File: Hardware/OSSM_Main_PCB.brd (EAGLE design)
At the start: 114.3 x 45.4 mm, 9 parts, among them J1 PJ-037AH, U1 LOLIN32_PRODUCTION

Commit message: Added Diode on 5V regulator
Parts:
- added D1: SS24FL, SS24FL:SODFL3617X108N
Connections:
- new net N$1: D1.A, PS1.3
- net 5V: now also D1.C; no longer PS1.3
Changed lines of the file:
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@@
 <attribute name="VALUE" x="55.245" y="52.07" size="1.27" layer="27" align="top-left"/>
+</element>
+<element name="D1" library="SS24FL" package="SODFL3617X108N" value="SS24FL" x="0" y="6.35" smashed="yes">
+<attribute name="DESCRIPTION" value=" Diode Schottky 40V 2A Surface Mount SOD-123F " x="0" y="6.35" size="1.778" layer="27" display="off"/>
+<attribute name="DIGI-KEY_PART_NUMBER" value="SS24FLCT-ND" x="0" y="6.35" size="1.778" layer="27" display="off"/>
+<attribute name="MF" value="ON Semiconductor" x="0" y="6.35" size="1.778" layer="27" display="off"/>
+<attribute name="MP" value="SS24FL" x="0" y="6.35" size="1.778" layer="27" display="off"/>
+<attribute name="NAME" x="-2.54" y="7.747" size="1.27" layer="25"/>
+<attribute name="PACKAGE" value="SOD-123 FL-2 ON Semiconductor" x="0" y="6.35" size="1.778" layer="27" display="off"/>
+<attribute name="PURCHASE-URL" value="https://pricing.snapeda.com/search/part/SS24FL/?ref=eda" x="0" y="6.35" size="1.778" layer="27" display="off"/>
+<attribute name="VALUE" x="-2.54" y="3.81" size="1.27" layer="27"/>
 </element>
 </elements>
@@
 </signal>
 <signal name="5V">
+<contactref element="D1" pad="C"/>
 <contactref element="U1" pad="15"/>
-<contactref element="PS1" pad="3"/>
-<wire x1="63.5" y1="54.9" x2="12.14" y2="74.93" width="0" layer="19" extent="1-1"/>
+<wire x1="-1.53" y1="6.35" x2="12.14" y2="74.93" width="0" layer="19" extent="1-1"/>
 </signal>
 <signal name="GND">
@@
 <wire x1="58.42" y1="54.9" x2="0" y2="41.91" width="0" layer="19" extent="1-1"/>
 </signal>
+<signal name="N$1">
+<contactref element="PS1" pad="3"/>
+<contactref element="D1" pad="A"/>
+<wire x1="1.53" y1="6.35" x2="63.5" y2="54.9" width="0" layer="19" extent="1-1"/>
+</signal>
 </signals>

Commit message: James' Attempt
Maybe made it better, maybe made it worse?
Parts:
- added C1: (no value), rcl:C050-024X044
- moved QWIIC_CONN 68.5 mm to (128.3, 53.3)
- moved STEPPER 66.8 mm to (91.4, 52.1)
- moved D1 64.5 mm to (54.6, 40.6), turned to 270 degrees
- moved 3.3V_CONN 64.4 mm to (134.6, 33.0), turned to 180 degrees
- moved MTR_CONN 61.8 mm to (100.3, 33.0), turned to 180 degrees
- moved IO_CONN 40.4 mm to (134.6, 72.4), turned to 180 degrees
- moved PS1 27.0 mm to (43.2, 36.8)
- moved GND_CONN 9.25 mm to (100.3, 72.4)
- moved J1 5.08 mm to (0.00, 36.8)
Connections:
- removed net VDD: STEPPER.10
- removed net VMOT: STEPPER.16
- new net N$10: MTR_CONN.4, STEPPER.13
- new net N$11: MTR_CONN.3, STEPPER.14
- new net N$12: IO_CONN.1, U1.13
- new net N$13: IO_CONN.2, U1.12
- new net N$14: IO_CONN.3, U1.11
- new net N$15: IO_CONN.4, U1.10
- new net N$16: IO_CONN.5, U1.9
- new net N$17: IO_CONN.6, U1.8
- new net N$2: STEPPER.1, U1.25
- new net N$3: STEPPER.2, U1.26
- new net N$4: STEPPER.3, U1.27
- new net N$5: STEPPER.4, U1.30
- new net N$6: STEPPER.7, U1.31
- new net N$7: STEPPER.8, U1.14
- new net N$8: MTR_CONN.6, STEPPER.11
- new net N$9: MTR_CONN.5, STEPPER.12
- net 24V: now also C1.2, STEPPER.16
- net 5V: now also STEPPER.10
- net GND: now also C1.1
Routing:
- net GND: track 0.00 -> 259.5 mm
- net 24V: track 0.00 -> 171.3 mm
- net 5V: track 0.00 -> 159.8 mm
- net N$12: track 0.00 -> 119.5 mm
- net N$13: track 0.00 -> 112.7 mm
- net N$14: track 0.00 -> 104.9 mm
- net N$15: track 0.00 -> 100.4 mm
- net 21_SDA: track 0.00 -> 96.0 mm
- net 22_SCL: track 0.00 -> 94.4 mm
- net N$16: track 0.00 -> 90.2 mm
- net N$17: track 0.00 -> 82.7 mm
- net N$5: track 0.00 -> 80.7 mm
- net N$6: track 0.00 -> 80.1 mm
- net N$4: track 0.00 -> 75.6 mm
- net N$3: track 0.00 -> 75.6 mm
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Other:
- board size 114.3 x 45.4 mm -> 143.5 x 51.7 mm

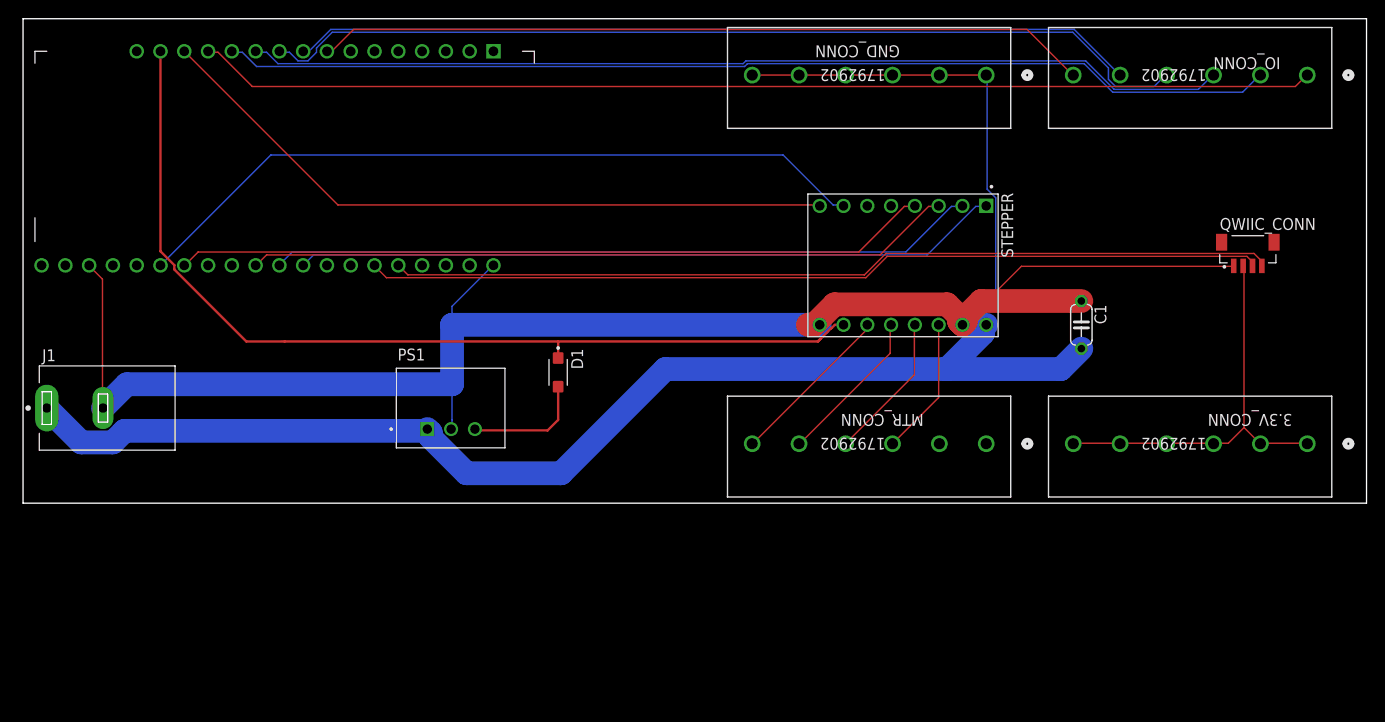
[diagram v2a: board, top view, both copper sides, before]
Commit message: beefed up ground, added PCB ground
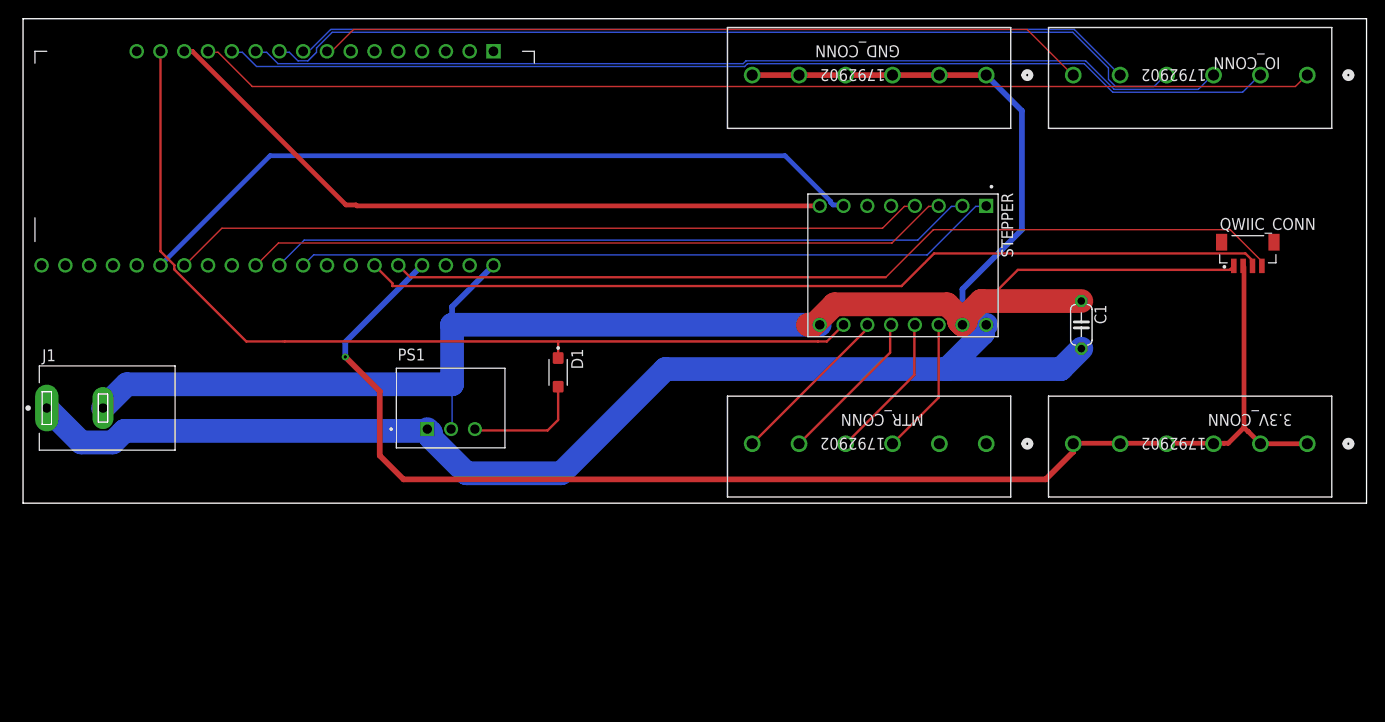
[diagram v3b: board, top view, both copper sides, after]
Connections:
- removed net 3V3: U1.1, U1.20, U1.29
- net 3_3V: now also U1.1, U1.20, U1.29
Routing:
- net 3_3V: track 43.9 -> 162.4 mm, vias 0 -> 1
- net N$7: track 74.7 -> 124.3 mm
- net GND: track 259.5 -> 271.2 mm
- net 22_SCL: track 94.4 -> 96.7 mm
- net 5V: track 159.8 -> 158.3 mm
- net 21_SDA: track 96.0 -> 97.2 mm

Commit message: Added holes, fixed 3.3V VIO
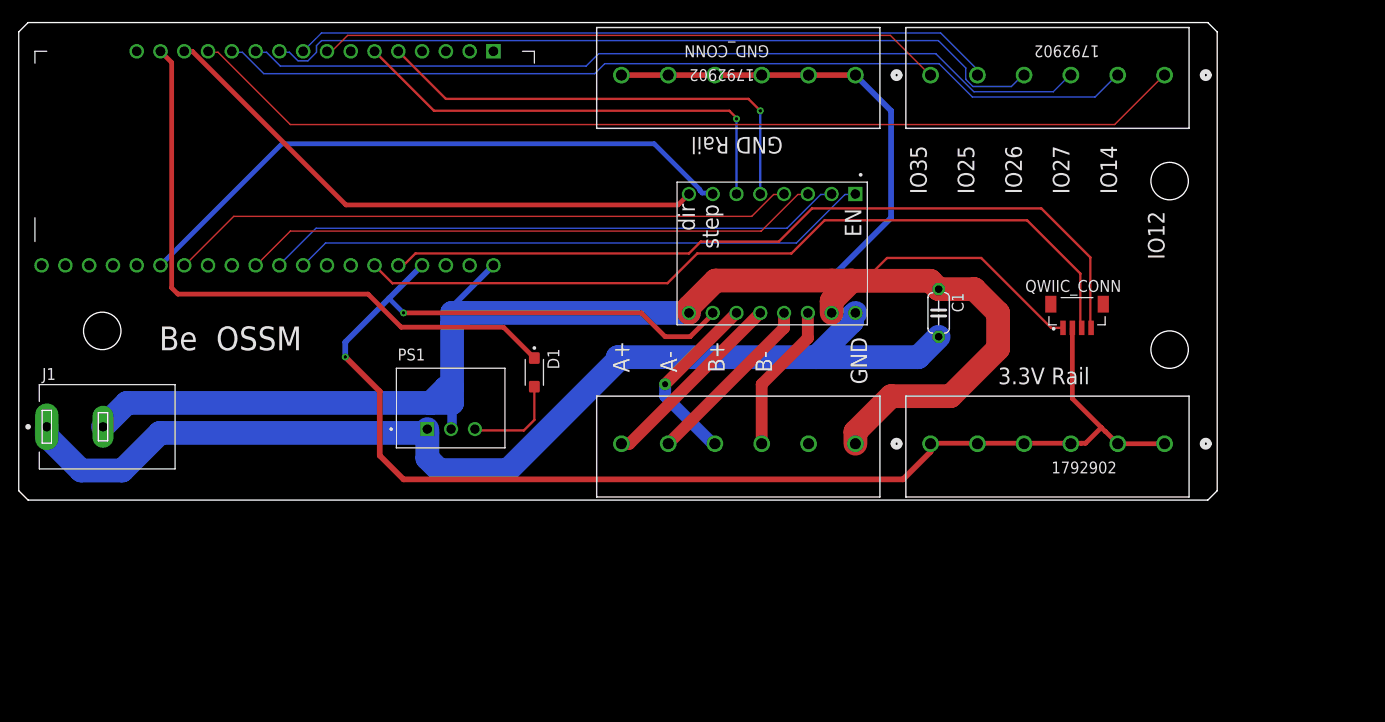
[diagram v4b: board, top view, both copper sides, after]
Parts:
- moved QWIIC_CONN 19.4 mm to (110.0, 46.7)
- moved C1 15.3 mm to (95.2, 47.0)
- moved 3.3V_CONN 15.2 mm to (119.4, 33.0)
- moved IO_CONN 15.2 mm to (119.4, 72.4)
- moved STEPPER 14.0 mm to (77.5, 53.3)
- moved GND_CONN 14.0 mm to (86.4, 72.4)
- moved MTR_CONN 14.0 mm to (86.4, 33.0)
- moved D1 2.54 mm to (52.1, 40.6)
- moved J1 2.00 mm to (0.00, 34.8)
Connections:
- new net IO32: STEPPER.5, U1.5
- new net IO33: STEPPER.6, U1.6
- net 3_3V: now also STEPPER.10
- net 5V: no longer STEPPER.10
- net GND: now also MTR_CONN.1
- net N$10: now also STEPPER.11; no longer STEPPER.13
- net N$8: now also STEPPER.12; no longer STEPPER.11
- net N$9: now also STEPPER.13; no longer STEPPER.12
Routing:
- net 5V: track 158.3 -> 67.6 mm
- net N$7: track 124.3 -> 61.3 mm
- net 24V: track 171.3 -> 120.5 mm
- net IO32: track 0.00 -> 50.2 mm, vias 0 -> 1
- net IO33: track 0.00 -> 49.7 mm, vias 0 -> 1
- net 3_3V: track 162.4 -> 179.3 mm, vias 1 -> 2
- net N$15: track 100.4 -> 84.6 mm
- net N$17: track 82.7 -> 66.9 mm
- net N$16: track 90.2 -> 75.0 mm
- net N$13: track 112.7 -> 98.5 mm
- net N$14: track 104.9 -> 90.7 mm
- net N$3: track 75.6 -> 62.2 mm
- net N$4: track 75.6 -> 62.2 mm
- net N$6: track 80.1 -> 66.7 mm
- net N$5: track 80.7 -> 67.2 mm
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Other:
- board size 143.5 x 51.7 mm -> 128 x 51 mm
- board text added: "3.3V Rail"
- board text added: "A+"
- board text added: "A-"
- board text added: "B+"
- board text added: "B-"
- board text added: "Be OSSM"
- board text added: "EN"
- board text added: "GND"
- board text added: "GND Rail"
- board text added: "IO12"
- board text added: "IO14"
- board text added: "IO25"
- board text added: "IO26"
- board text added: "IO27"
- board text added: "IO35"
- board text added: "dir"
- board text added: "step"

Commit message: Motor 24v + KM marking
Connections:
- net 24V: now also MTR_CONN.2
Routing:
- net 24V: track 120.5 -> 130.8 mm
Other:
- board text added: "KinkyMakers.com"
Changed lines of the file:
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@@
 <?xml version="1.0" encoding="utf-8"?>
 <!DOCTYPE eagle SYSTEM "eagle.dtd">
-<eagle version="9.6.1">
+<eagle version="9.6.2">
 <drawing>
 <settings>
@@
 </layers>
 <board>
-<fusionsync huburn="a.cGVyc29uYWw6dWUyYzQ4Yzk0" projecturn="a.cGVyc29uYWw6dWUyODJhZTcyIzIwMTkxMDAxMjIxMDYwMzgx" f3durn="urn:adsk.wipprod:dm.lineage:1fqrZAinQcCWnb5WX0o0Jg" pcbguid="" lastpulledtime="" lastsyncedchangeguid="" latestrevisionid="936eb7c4-54d2-4e20-9cf5-19f87d9b7519" lastsyncedrevisionid="936eb7c4-54d2-4e20-9cf5-19f87d9b7519" lastboardhashguid="c1262d79-7258-d3c1-be9d-ffa79a74015f" lastpushedtime="2021-04-05T14:20:12Z" linktopcb3d="%12"/>
+<fusionsync huburn="a.cGVyc29uYWw6dWUyYzQ4Yzk0" projecturn="a.cGVyc29uYWw6dWUyODJhZTcyIzIwMTkxMDAxMjIxMDYwMzgx" f3durn="urn:adsk.wipprod:dm.lineage:1fqrZAinQcCWnb5WX0o0Jg" pcbguid="" lastpulledtime="" lastsyncedchangeguid="" latestrevisionid="936eb7c4-54d2-4e20-9cf5-19f87d9b7519" lastsyncedrevisionid="936eb7c4-54d2-4e20-9cf5-19f87d9b7519" lastboardhashguid="c1262d79-7258-d3c1-be9d-ffa79a74015f" lastpushedtime="2021-04-05T14:20:12Z" linktopcb3d="true"/>
 <plain>
 <text x="62.23" y="40.64" size="1.778" layer="21" rot="R90">A+</text>
@@
 <hole x="119.92" y="43.07" drill="4"/>
 <hole x="5.92" y="45.07" drill="4"/>
-<text x="12" y="43" size="2.54" layer="21">Be  OSSM</text>
+<text x="11" y="45" size="2.54" layer="21">Be  OSSM</text>
+<text x="10" y="42" size="1.778" layer="25">KinkyMakers.com</text>
 </plain>
 <attributes>
@@
 <wire x1="86.36" y1="72.39" x2="61.3664" y2="72.39" width="0.6096" layer="1"/>
 <wire x1="108.53" y1="45.395" x2="107.26" y2="45.395" width="0.254" layer="1"/>
-<wire x1="107.26" y1="45.395" x2="99.7976" y2="52.8574" width="0.254" layer="1"/>
+<wire x1="107.26" y1="45.395" x2="99.8275" y2="52.8275" width="0.254" layer="1"/>
+<wire x1="99.8275" y1="52.8275" x2="99.7976" y2="52.8574" width="0.254" layer="1"/>
 <wire x1="99.7976" y1="52.8574" x2="89.7382" y2="52.8574" width="0.254" layer="1"/>
 <wire x1="89.7382" y1="52.8574" x2="87.6554" y2="50.7746" width="0.254" layer="1"/>
@@
 <wire x1="60.98120625" y1="42.2626" x2="82.18605625" y2="42.2626" width="2.54" layer="16"/>
 <contactref element="C1" pad="2"/>
-<wire x1="82.18605625" y1="42.2626" x2="93.0626" y2="42.2626" width="2.54" layer="16"/>
+<wire x1="82.18605625" y1="42.2626" x2="84" y2="42.2626" width="2.54" layer="16"/>
+<wire x1="84" y1="42.2626" x2="93.0626" y2="42.2626" width="2.54" layer="16"/>
 <wire x1="93.0626" y1="42.2626" x2="95.25" y2="44.45" width="2.54" layer="16"/>
 <wire x1="40.64" y1="34.1696" x2="40.64" y2="31.48" width="2.54" layer="16"/>
@@
 <wire x1="0" y1="33.83" x2="3.6724" y2="30.1576" width="2.54" layer="16"/>
 <wire x1="40.64" y1="34.58" x2="40.64" y2="34.1696" width="2.54" layer="16"/>
+<contactref element="MTR_CONN" pad="2"/>
+<wire x1="81.3562" y1="33.02" x2="81.3562" y2="39.6188" width="2.54" layer="16"/>
+<wire x1="81.3562" y1="39.6188" x2="84" y2="42.2626" width="2.54" layer="16"/>
 </signal>
 <signal name="N$1">
